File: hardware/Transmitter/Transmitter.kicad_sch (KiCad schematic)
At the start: 102 parts, among them IC1 ESP32-C3-MINI-1-N4, J1 USB_C_Receptacle_USB2.0, J2 UP_BTN, J3 DN_BTN, J3 UART, J4 Conn_01x03, J6 JST_PH, Q1 2N7002, Q10 NChan, Q11 NChan, Q2 NChan, Q3 NChan, Q4 NChan, Q5 PChan, Q6 PChan, Q7 PChan, Q8 NChan, Q9 NChan, SW1 Reset, SW2 SW_SPST, U1 TPS22810DRV, U2 TPS22810DRV, U3 AZ1117-3.3

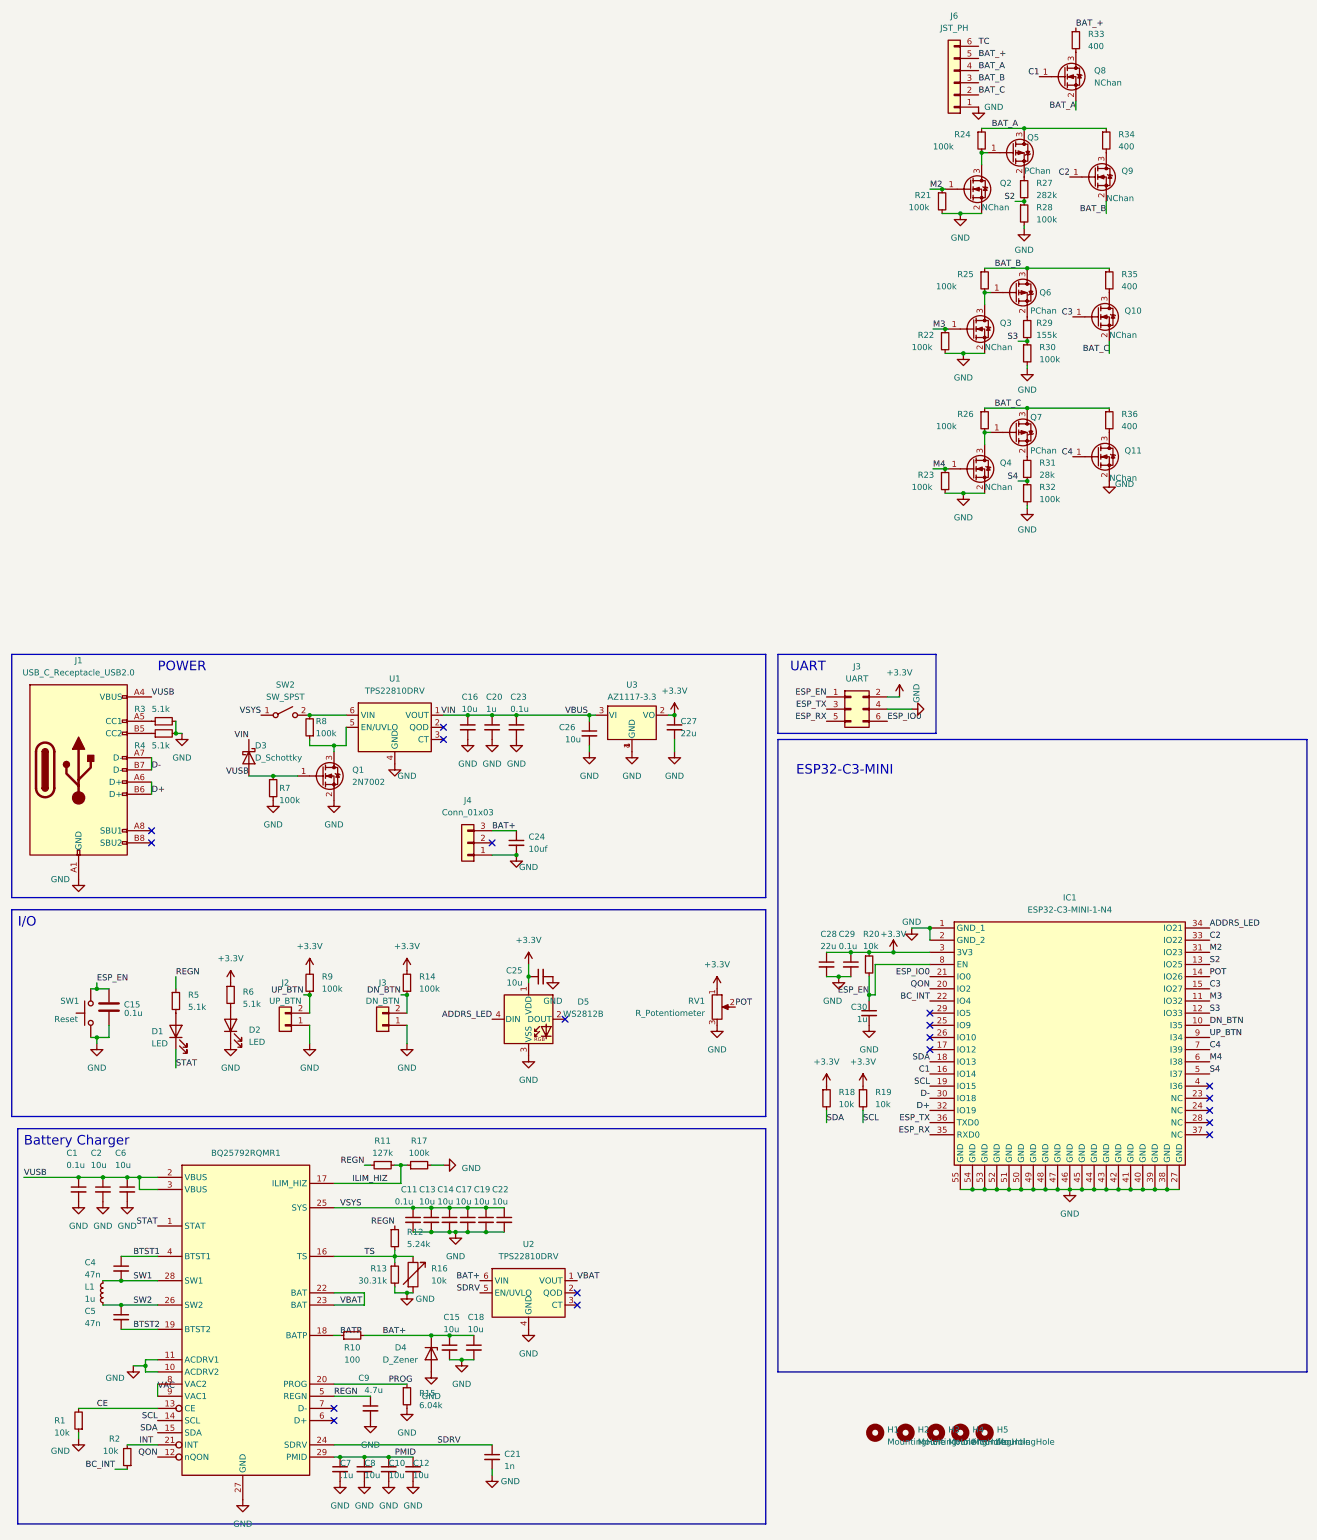
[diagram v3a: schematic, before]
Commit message: BMS added to hardware
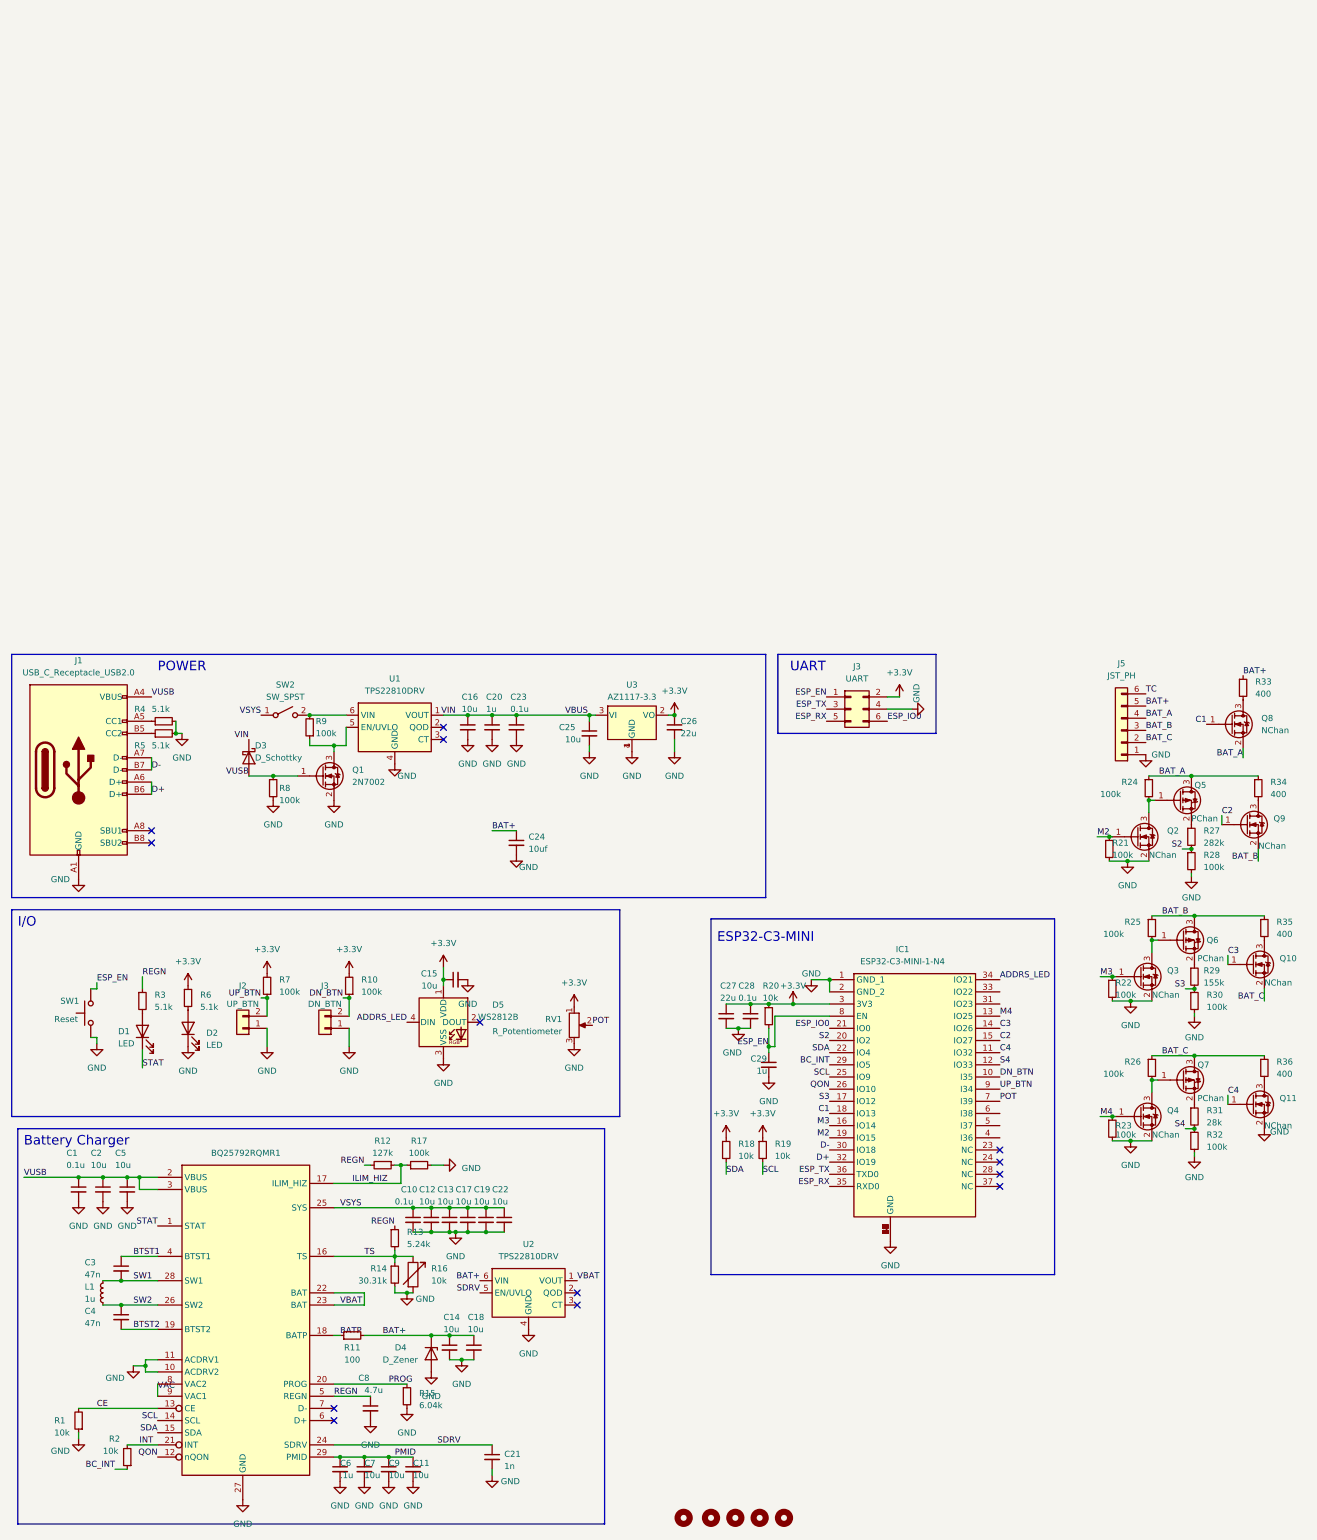
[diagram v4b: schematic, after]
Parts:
- removed C15: 0.1u, Capacitor_SMD:C_0402_1005Metric, symbol Device:C
- removed J4: Conn_01x03, Connector_JST:JST_PH_B3B-PH-K_1x03_P2.00mm_Vertical, symbol Connector_Generic:Conn_01x03
- removed J6: JST_PH, Connector_JST:JST_PH_B6B-PH-K_1x06_P2.00mm_Vertical, symbol Connector_Generic:Conn_01x06
- added J5: JST_PH, Connector_JST:JST_PH_B6B-PH-K_1x06_P2.00mm_Vertical, symbol Connector_Generic:Conn_01x06
- renumbered C11 to C10, C12 to C11, C13 to C12, C14 to C13, C15 to C14, C25 to C15, C26 to C25, C27 to C26, C28 to C27, C29 to C28, C30 to C29, C4 to C3, C5 to C4, C6 to C5, C7 to C6, C8 to C7, C9 to C8, C10 to C9, R14 to R10, R10 to R11, R11 to R12, R12 to R13, R13 to R14, R5 to R3, R3 to R4, R4 to R5, R9 to R7, R7 to R8, R8 to R9
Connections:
- net BAT_+ is gone; now on net BAT+: R33.1
- net BAT+: now also J5.5 (Pin_5)
- net BAT_A: now also J5.4 (Pin_4)
- net BAT_B: now also J5.3 (Pin_3)
- net BAT_C: now also J5.2 (Pin_2)
- net BC_INT: now also IC1.29 (IO5); no longer IC1.22 (IO4)
- net C1: now also IC1.18 (IO13); no longer IC1.16 (IO14)
- net C2: now also IC1.15 (IO27); no longer IC1.33 (IO22)
- net C3: now also IC1.14 (IO26); no longer IC1.15 (IO27)
- net C4: now also IC1.11 (IO32); no longer IC1.7 (I39)
- net GND: now also J5.1 (Pin_1)
- net M2: now also IC1.19 (IO15); no longer IC1.31 (IO23)
- net M3: now also IC1.16 (IO14); no longer IC1.11 (IO32)
- net M4: now also IC1.13 (IO25); no longer IC1.6 (I38)
- net POT: now also IC1.7 (I39); no longer IC1.14 (IO26)
- net QON: now also IC1.26 (IO10); no longer IC1.20 (IO2)
- net S2: now also IC1.20 (IO2); no longer IC1.13 (IO25)
- net S3: now also IC1.17 (IO12); no longer IC1.12 (IO33)
- net S4: now also IC1.12 (IO33); no longer IC1.5 (I37)
- net SCL: now also IC1.25 (IO9); no longer IC1.19 (IO15)
- net SDA: now also IC1.22 (IO4); no longer IC1.18 (IO13)
- net TC: now also J5.6 (Pin_6)
- no-connect marks 19 -> 13
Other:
- moved on the sheet: C15, C27, C28, C29, D1, D2, D5, J2, J3, R10, R18, R19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

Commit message: rename battery leads, update footprints
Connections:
- net BAT_A renamed BAT_C3
- net BAT_B renamed BAT_C2
- net BAT_C renamed BAT_C1
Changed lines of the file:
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@@
     (effects (font (size 1.27 1.27)) (justify left bottom))
   )
-  (label "BAT_A" (at 269.875 35.56 180) (fields_autoplaced)
+  (label "BAT_C3" (at 269.875 35.56 180) (fields_autoplaced)
     (effects (font (size 1.27 1.27)) (justify right bottom))
   )
@@
     (effects (font (size 1.27 1.27)) (justify right bottom))
   )
+  (label "BAT_C2" (at 249.555 29.845 0) (fields_autoplaced)
+    (effects (font (size 1.27 1.27)) (justify left bottom))
+  )
   (label "VBAT" (at 130.81 144.78 0) (fields_autoplaced)
     (effects (font (size 1.27 1.27)) (justify left bottom))
   )
-  (label "BAT_C" (at 258.445 97.79 180) (fields_autoplaced)
+  (label "BAT_C1" (at 258.445 97.79 180) (fields_autoplaced)
     (effects (font (size 1.27 1.27)) (justify right bottom))
   )
@@
     (effects (font (size 1.27 1.27)) (justify left bottom))
   )
+  (label "BAT_C1" (at 249.555 32.385 0) (fields_autoplaced)
+    (effects (font (size 1.27 1.27)) (justify left bottom))
+  )
   (label "M4" (at 240.03 110.49 0) (fields_autoplaced)
     (effects (font (size 1.27 1.27)) (justify left bottom))
@@
     (effects (font (size 1.27 1.27)) (justify right bottom))
   )
-  (label "BAT_A" (at 257.81 39.37 180) (fields_autoplaced)
-    (effects (font (size 1.27 1.27)) (justify right bottom))
-  )
-  (label "BAT_A" (at 249.555 27.305 0) (fields_autoplaced)
-    (effects (font (size 1.27 1.27)) (justify left bottom))
-  )
-  (label "BAT_C" (at 274.32 86.36 180) (fields_autoplaced)
+  (label "BAT_C3" (at 257.81 39.37 180) (fields_autoplaced)
+    (effects (font (size 1.27 1.27)) (justify right bottom))
+  )
+  (label "BAT_C1" (at 274.32 86.36 180) (fields_autoplaced)
     (effects (font (size 1.27 1.27)) (justify right bottom))
   )
@@
     (effects (font (size 1.27 1.27)) (justify left bottom))
   )
-  (label "BAT_B" (at 249.555 29.845 0) (fields_autoplaced)
-    (effects (font (size 1.27 1.27)) (justify left bottom))
-  )
   (label "SDRV" (at 101.6 179.07 0) (fields_autoplaced)
     (effects (font (size 1.27 1.27)) (justify left bottom))
   )
-  (label "BAT_B" (at 273.05 57.15 180) (fields_autoplaced)
+  (label "BAT_C2" (at 273.05 57.15 180) (fields_autoplaced)
     (effects (font (size 1.27 1.27)) (justify right bottom))
   )
@@
     (effects (font (size 1.27 1.27)) (justify left bottom))
   )
-  (label "BAT_B" (at 258.445 68.58 180) (fields_autoplaced)
-    (effects (font (size 1.27 1.27)) (justify right bottom))
-  )
-  (label "BAT_C" (at 249.555 32.385 0) (fields_autoplaced)
-    (effects (font (size 1.27 1.27)) (justify left bottom))
+  (label "BAT_C2" (at 258.445 68.58 180) (fields_autoplaced)
+    (effects (font (size 1.27 1.27)) (justify right bottom))
   )
   (label "BAT+" (at 110.49 144.78 180) (fields_autoplaced)
@@
     (effects (font (size 1.27 1.27)) (justify left bottom))
   )
+  (label "BAT_C3" (at 249.555 27.305 0) (fields_autoplaced)
+    (effects (font (size 1.27 1.27)) (justify left bottom))
+  )

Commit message: add battery balancing to transmitter
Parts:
- removed IC1: ESP32-C3-MINI-1-N4, ESP32MINI1N4:ESP32MINI1N4, symbol ESP32-C3-MINI-1-N4:ESP32-C3-MINI-1-N4
- removed J5: JST_PH, Connector_JST:JST_PH_B6B-PH-K_1x06_P2.00mm_Vertical, symbol Connector_Generic:Conn_01x06
- removed Q10, Q11, Q2, Q3, Q4, Q8, Q9: NChan, Package_TO_SOT_SMD:SOT-23, symbol Transistor_FET:DMG3418L
- removed Q5, Q6, Q7: PChan, Package_TO_SOT_SMD:SOT-23, symbol Transistor_FET:BSS83P
- removed R21, R22, R23, R24, R25, R26, R28, R30, R32: 100k, Resistor_SMD:R_0402_1005Metric, symbol Device:R_Small
- removed R27: 282k, Resistor_SMD:R_0402_1005Metric, symbol Device:R_Small
- removed R29: 155k, Resistor_SMD:R_0402_1005Metric, symbol Device:R_Small
- removed R31: 28k, Resistor_SMD:R_0402_1005Metric, symbol Device:R_Small
- removed R33, R34, R35, R36: 400, Resistor_SMD:R_2010_5025Metric, symbol Device:R_Small
- added BT1, BT2, BT3, BT4: Battery_Cell, symbol Device:Battery_Cell
- added C30, C31, C32, C33, C34: 220nf, Capacitor_SMD:C_0402_1005Metric, symbol Device:C_Small
- added C35: 100p, Capacitor_SMD:C_0402_1005Metric, symbol Device:C
- added C36: 0.1u, Capacitor_SMD:C_0402_1005Metric, symbol Device:C
- added C37, C38: 1u, Capacitor_SMD:C_0402_1005Metric, symbol Device:C_Small
- added C39, C40: 0.1u, Capacitor_SMD:C_0402_1005Metric, symbol Device:C_Small
- added D6, D7, D8, D9: 1N4148WQ-13-F, Diode_SMD:D_SOD-123, symbol Device:D_Zener
- added J6: JST_PH, Connector_JST:JST_PH_B6B-PH-K_1x06_P2.00mm_Vertical, symbol Connector_Generic:Conn_01x06
- added JP1: BQ76905_Bypass, Jumper:SolderJumper-2_P1.3mm_Open_RoundedPad1.0x1.5mm, symbol Jumper:SolderJumper_2_Open
- added Q12, Q13: NMOS, Package_TO_SOT_SMD:SOT-23, symbol Simulation_SPICE:NMOS
- added Q14: PMOS, Package_TO_SOT_SMD:SOT-23, symbol Simulation_SPICE:PMOS
- added R37, R38, R39, R40, R41: 10, Resistor_SMD:R_0402_1005Metric, symbol Device:R_Small
- added R42, R44, R45: 100, Resistor_SMD:R_0402_1005Metric, symbol Device:R_Small
- added R43: 1m, Resistor_SMD:R_0402_1005Metric, symbol Device:R_Small
- added R46: 0, Resistor_SMD:R_0402_1005Metric, symbol Device:R_Small
- added R47, R48: 5.1k, Resistor_SMD:R_0402_1005Metric, symbol Device:R_Small
- added R49: 100k, Resistor_SMD:R_0402_1005Metric, symbol Device:R_Small
- added SW1: Boot, Switch:Tactile_5.5mmx2.85mm, symbol Switch:SW_Push
- added U4: ESP32-S3-MINI-1-N8, XCVR_ESP32-S3-MINI-1-N8:XCVR_ESP32-S3-MINI-1-N8, symbol ESP32-S3-MINI-1-N8:ESP32-S3-MINI-1-N8
- added U5: ~, Package_DFN_QFN:UQFN-20-1EP_3x3mm_P0.4mm_EP1.85x1.85mm, symbol Battery_Management_:BQ76905
- J3: footprint Connector_PinHeader_1.27mm:PinHeader_2x03_P1.27mm_Vertical -> (none)
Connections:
- net +3.3V: now also Q14.2 (G), U4.3 (3V3)
- net ADDRS_LED: now also U4.5 (IO1)
- net BAT+: now also BT1.1 (+), D6.2 (A), D7.2 (A), J6.5 (Pin_5), R37.1
- net BAT_C1: now also BT3.2 (-), BT4.1 (+), J6.2 (Pin_2), R40.1
- net BAT_C2: now also BT2.2 (-), BT3.1 (+), J6.3 (Pin_3), R39.1
- net BAT_C3: now also BT1.2 (-), BT2.1 (+), J6.4 (Pin_4), R38.1
- net BC_INT: now also U4.31 (IO35)
- net C1: now also U4.25 (IO21)
- net C2: now also U4.20 (IO16)
- net C3: now also U4.19 (IO15)
- net C4: now also U4.16 (IO12)
- net D+: now also U4.24 (IO20/D+)
- net D-: now also U4.23 (IO19/D-)
- net DN_BTN: now also U4.11 (IO7)
- net ESP_EN: now also U4.45 (EN)
- net ESP_IO0: now also SW1.2, U4.4 (IO0_BOOT0)
- net ESP_RX: now also U4.40 (RXD0)
- net ESP_TX: now also U4.39 (TXD0)
- net GND: now also C34.2, C37.2, C38.2, C40.2, D9.2 (A), JP1.2 (B), Q13.3 (S), R49.1, SW1.1, U4.1 (GND), U4.2 (GND), U4.42 (GND), U4.43 (GND), U4.46 (GND), U4.47 (GND), U4.48 (GND), U4.49 (GND), U4.50 (GND), U4.51 (GND), U4.52 (GND), U4.53 (GND), U4.54 (GND), U4.55 (GND), U4.56 (GND), U4.57 (GND), U4.58 (GND), U4.59 (GND), U4.60 (GND), U4.61 (EXP), U4.62 (GND), U4.63 (GND), U4.64 (GND), U4.65 (GND), U4.66 (EXP), U4.67 (EXP), U4.68 (EXP), U4.69 (EXP), U4.70 (EXP), U4.71 (EXP), U4.72 (EXP), U4.73 (EXP), U5.11 (VSS), U5.21 (VSS)
- net M2: now also U4.26 (IO26)
- net M3: now also U4.21 (IO17/DAC1)
- net M4: now also U4.18 (IO14)
- net POT: now also U4.15 (IO11)
- net QON: now also U4.30 (IO48)
- net S2: now also U4.27 (IO47)
- net S3: now also U4.22 (IO18/DAC2)
- net S4: now also U4.17 (IO13)
- net SCL: now also U4.29 (IO34), U5.12 (SCL)
- net SDA: now also U4.28 (IO33), U5.13 (SDA)
- net TS: now also D8.1 (K), J6.6 (Pin_6), U5.8 (TS); no longer BQ25792RQMR1.16 (TS), R13.2, R14.1, R16.1
- net UP_BTN: now also U4.8 (IO4)
- new net: C38.1, R46.2, U5.16 (REGSRC)
- new net: D7.1 (K), R46.1
- new net: C37.1, R44.2, U5.17 (BAT)
- new net: BQ25792RQMR1.16 (TS), R13.2, R14.1, R16.1
- new net: D6.1 (K), R44.1
- new net: C39.1, Q12.3 (S), R43.2, R45.2
- new net: C35.1, C36.1, R42.1, U5.7 (SRN)
- new net: C35.2, C36.2, R45.1, U5.6 (SRP)
- new net: C39.2, C40.1
- new net: D8.2 (A), Q14.1 (D)
- new net: R48.1, U5.10 (CHG)
- new net: D9.1 (K), Q13.2 (G), R48.2, R49.2
- new net: R47.1, U5.9 (DSG)
- new net: Q12.2 (G), R47.2
- new net: Q12.1 (D), Q13.1 (D)
- new net ALERT: U5.14 (ALERT)
- new net BAT_C0: BT4.2 (-), J6.1 (Pin_1), JP1.1 (A), R41.1, R42.2, R43.1
- new net VC0: C33.2, C34.1, R41.2, U5.5 (VC0)
- new net VC1: C32.2, C33.1, R40.2, U5.4 (VC1)
- new net VC2: C31.2, C32.1, R39.2, U5.1 (VC3A), U5.2 (VC3B), U5.3 (VC2)
- new net VC3: C30.2, C31.1, R38.2, U5.19 (VC4A), U5.20 (VC4B)
- new net VC4: C30.1, R37.2, U5.18 (VC5)
- new net WAKE: Q14.3 (S)
- no-connect marks 13 -> 26
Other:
- note added: "Cell Balancing"
- moved on the sheet: C27, C28, C29, R18, R19, R20, SW1

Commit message: create bom
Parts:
- H1, H2, H3, H4, H5: footprint MountingHole:MountingHole_2.2mm_M2 -> MountingHole:MountingHole_3.2mm_M3_DIN965_Pad_TopBottom
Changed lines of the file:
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@@
       (effects (font (size 1.27 1.27)) (justify left) hide)
     )
-    (property "Footprint" "MountingHole:MountingHole_2.2mm_M2" (at 173.99 194.31 0)
+    (property "Footprint" "MountingHole:MountingHole_3.2mm_M3_DIN965_Pad_TopBottom" (at 173.99 194.31 0)
       (effects (font (size 1.27 1.27)) hide)
     )
@@
       (effects (font (size 1.27 1.27)) (justify left) hide)
     )
-    (property "Footprint" "MountingHole:MountingHole_2.2mm_M2" (at 168.91 194.31 0)
+    (property "Footprint" "MountingHole:MountingHole_3.2mm_M3_DIN965_Pad_TopBottom" (at 168.91 194.31 0)
       (effects (font (size 1.27 1.27)) hide)
     )
@@
       (effects (font (size 1.27 1.27)) (justify left) hide)
     )
-    (property "Footprint" "MountingHole:MountingHole_2.2mm_M2" (at 153.035 194.31 0)
+    (property "Footprint" "MountingHole:MountingHole_3.2mm_M3_DIN965_Pad_TopBottom" (at 153.035 194.31 0)
       (effects (font (size 1.27 1.27)) hide)
     )
@@
       (effects (font (size 1.27 1.27)) (justify left) hide)
     )
-    (property "Footprint" "MountingHole:MountingHole_2.2mm_M2" (at 158.75 194.31 0)
+    (property "Footprint" "MountingHole:MountingHole_3.2mm_M3_DIN965_Pad_TopBottom" (at 158.75 194.31 0)
       (effects (font (size 1.27 1.27)) hide)
     )
@@
       (effects (font (size 1.27 1.27)) (justify left) hide)
     )
-    (property "Footprint" "MountingHole:MountingHole_2.2mm_M2" (at 163.83 194.31 0)
+    (property "Footprint" "MountingHole:MountingHole_3.2mm_M3_DIN965_Pad_TopBottom" (at 163.83 194.31 0)
       (effects (font (size 1.27 1.27)) hide)
     )

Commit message: PCB revision
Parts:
- removed C19, C22: 10u, Capacitor_SMD:C_0603_1608Metric, symbol Device:C_Small
- added D10, D11, D12, D13, D14: TVN3V3B1S, Diode_SMD:D_0402_1005Metric, symbol Device:D_TVS
- added R22: 10k, Resistor_SMD:R_0402_1005Metric, symbol Device:R_Small
- C11, C12, C13, C14, C15, C17, C18, C2, C5, C7, C9: footprint Capacitor_SMD:C_0603_1608Metric -> Capacitor_SMD:C_0805_2012Metric
- C16: footprint Capacitor_SMD:C_0402_1005Metric -> Capacitor_SMD:C_0805_2012Metric
- D3: value D_Schottky -> EVVOSS16
- D6, D7, D8, D9: footprint Diode_SMD:D_SOD-123 -> Diode_SMD:D_SOD-323
- L1: footprint Inductor_SMD:L_Sunlord_MWSA0402S -> Inductor_SMD:L_1008_2520Metric
- RV1: footprint Potentiometer_THT:Potentiometer_Alps_RK09L_Single_Vertical -> Potentiometer:Potentiometer_Bourns_PVT111-3
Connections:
- net +3.3V: now also R22.1
- net D+: now also D12.2 (A2)
- net D-: now also D13.2 (A2)
- net ESP_EN: now also D11.2 (A2)
- net ESP_IO0: now also D10.2 (A2)
- net GND: now also D10.1 (A1), D11.1 (A1), D12.1 (A1), D13.1 (A1), D14.2 (A2)
- net at R9.2, SW2.2 (B), U1.6 (VIN): now also D14.1 (A1)
- net S3: no longer names the net of U4.22 (IO18/DAC2)
- net S3: now also R22.2
